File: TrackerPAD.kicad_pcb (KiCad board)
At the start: 2 copper layers, 61.1 x 63 mm, 6 parts, among them J1 Conn_01x06, J2 Conn_01x06, U1 ViveTracker-holes, U2 ViveTracker, U3 ViveTracker, U4 ViveTracker

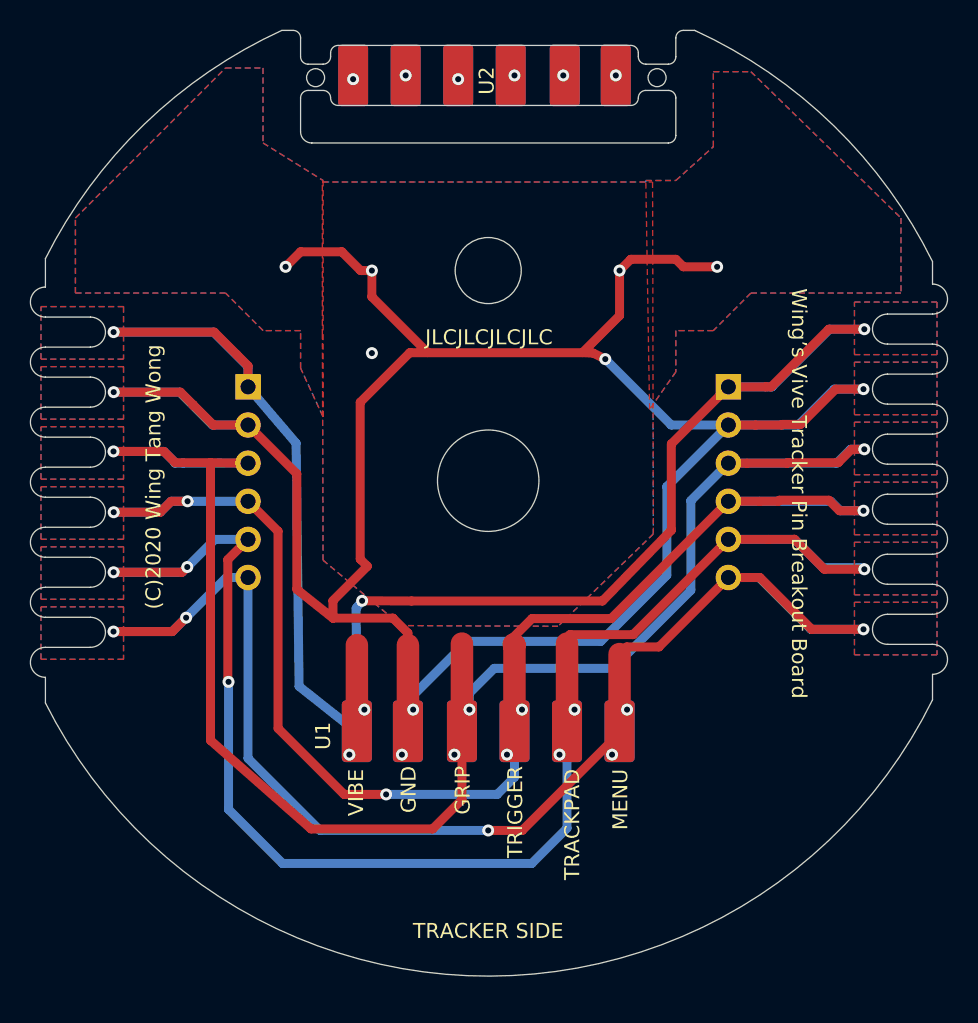
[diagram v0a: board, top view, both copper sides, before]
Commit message: Added M3 mount bracket positions. Moved some traces and vias. Added ground plane for other half of board.
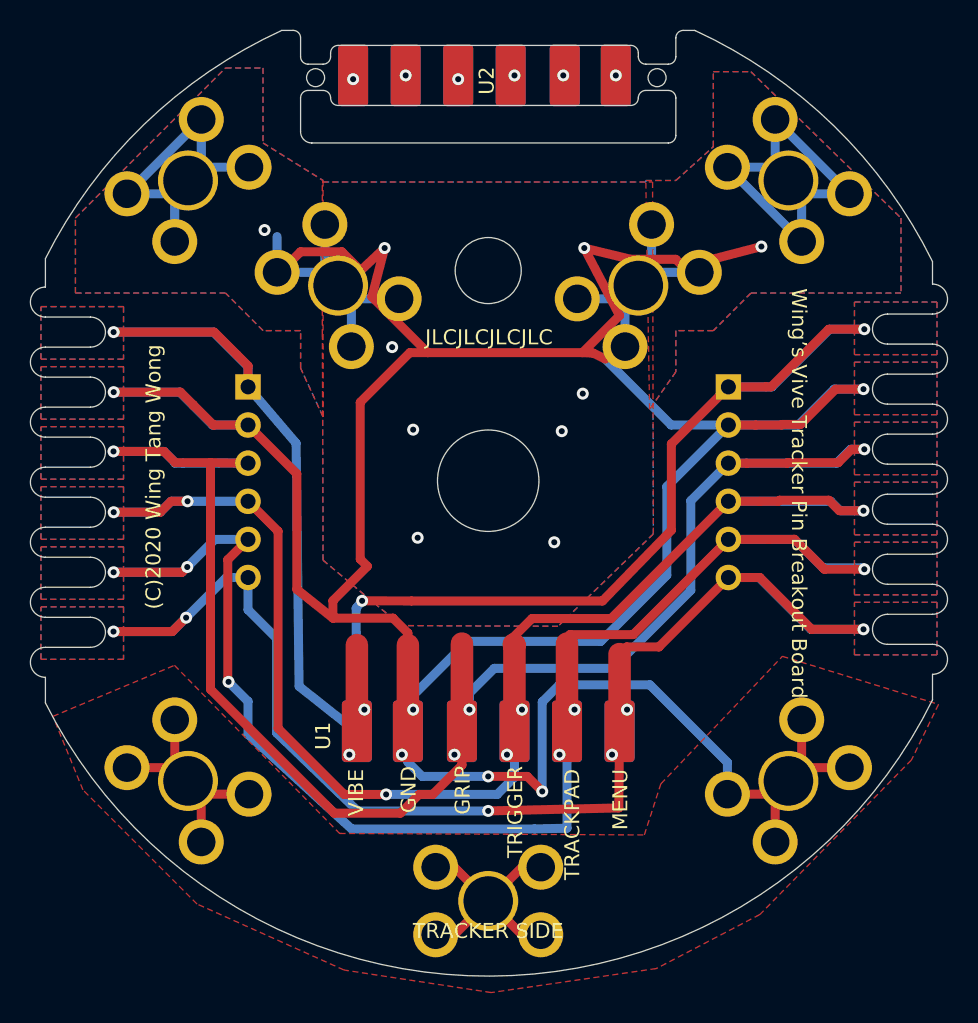
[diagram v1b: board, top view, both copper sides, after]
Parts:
- added M1: M3MountLugHole, WingCustomParts:M3-Mount-Lug-Hole, B.Cu at (20.0, -20.0)
- added M2: M3MountLugHole, WingCustomParts:M3-Mount-Lug-Hole, B.Cu at (-20.0, -20.0)
- added M3: M3MountLugHole, WingCustomParts:M3-Mount-Lug-Hole, B.Cu at (10.0, -13.0)
- added M4: M3MountLugHole, WingCustomParts:M3-Mount-Lug-Hole, B.Cu at (-10.0, -13.0)
- added M5: M3MountLugHole, WingCustomParts:M3-Mount-Lug-Hole, B.Cu at (-20.0, 20.0)
- added M6: M3MountLugHole, WingCustomParts:M3-Mount-Lug-Hole, B.Cu at (20.0, 20.0)
- added M7: M3MountLugHole, WingCustomParts:M3-Mount-Lug-Hole, B.Cu at (0.00, 28.0)
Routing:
- net GND: track 174.3 -> 352.0 mm, vias 10 -> 15
- net TRACKPAD: track 104.4 -> 98.6 mm
- net GRIP: track 114.5 -> 110.5 mm
- net (no net): vias 0 -> 1
